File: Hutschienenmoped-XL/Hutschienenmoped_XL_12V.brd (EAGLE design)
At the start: 96.3 x 101.8 mm, 118 parts, among them J1 638207222005, J13 638207222005, J15 638207222008, J2 645004114822, J3 61302211821, J4 61300421121, J6 61302211821, J7 638207222005, J8 638207222007, U1 ESP32-S3-DEVKITC-1-N8R2, U4 TLE9250VSJ

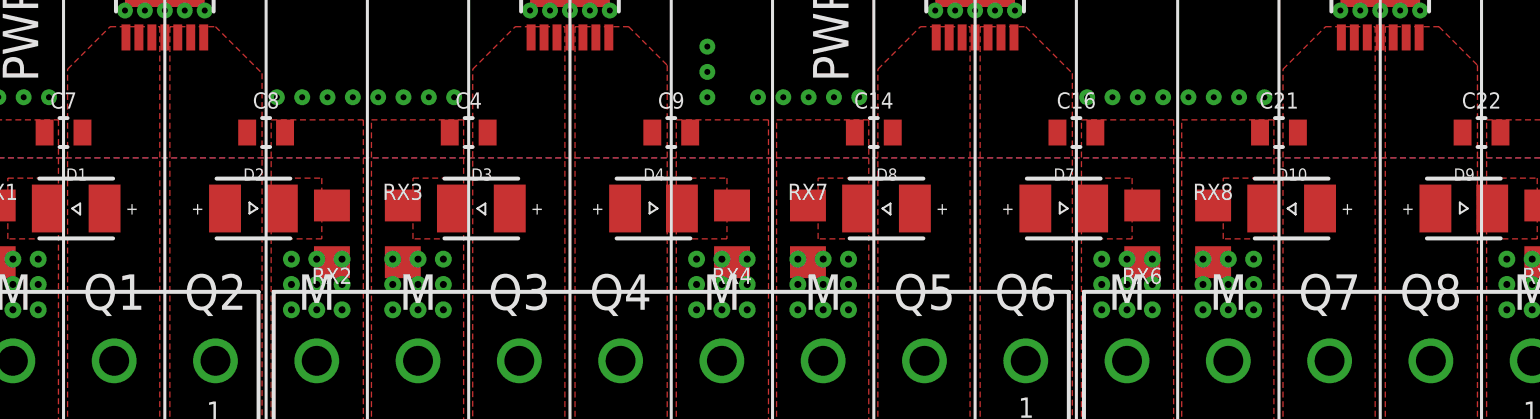
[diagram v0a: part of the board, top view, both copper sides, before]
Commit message: update Libraries.
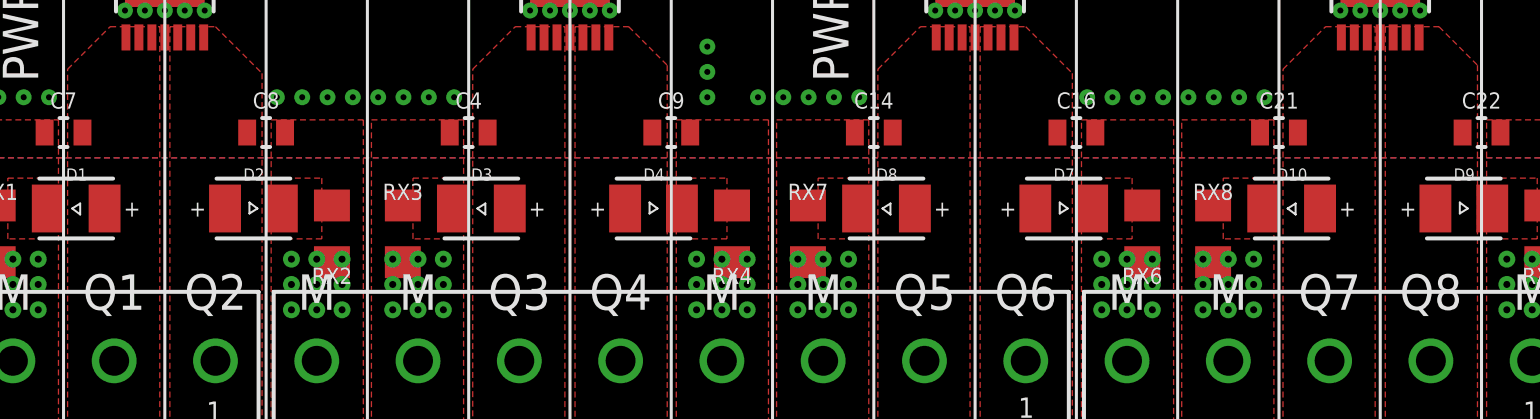
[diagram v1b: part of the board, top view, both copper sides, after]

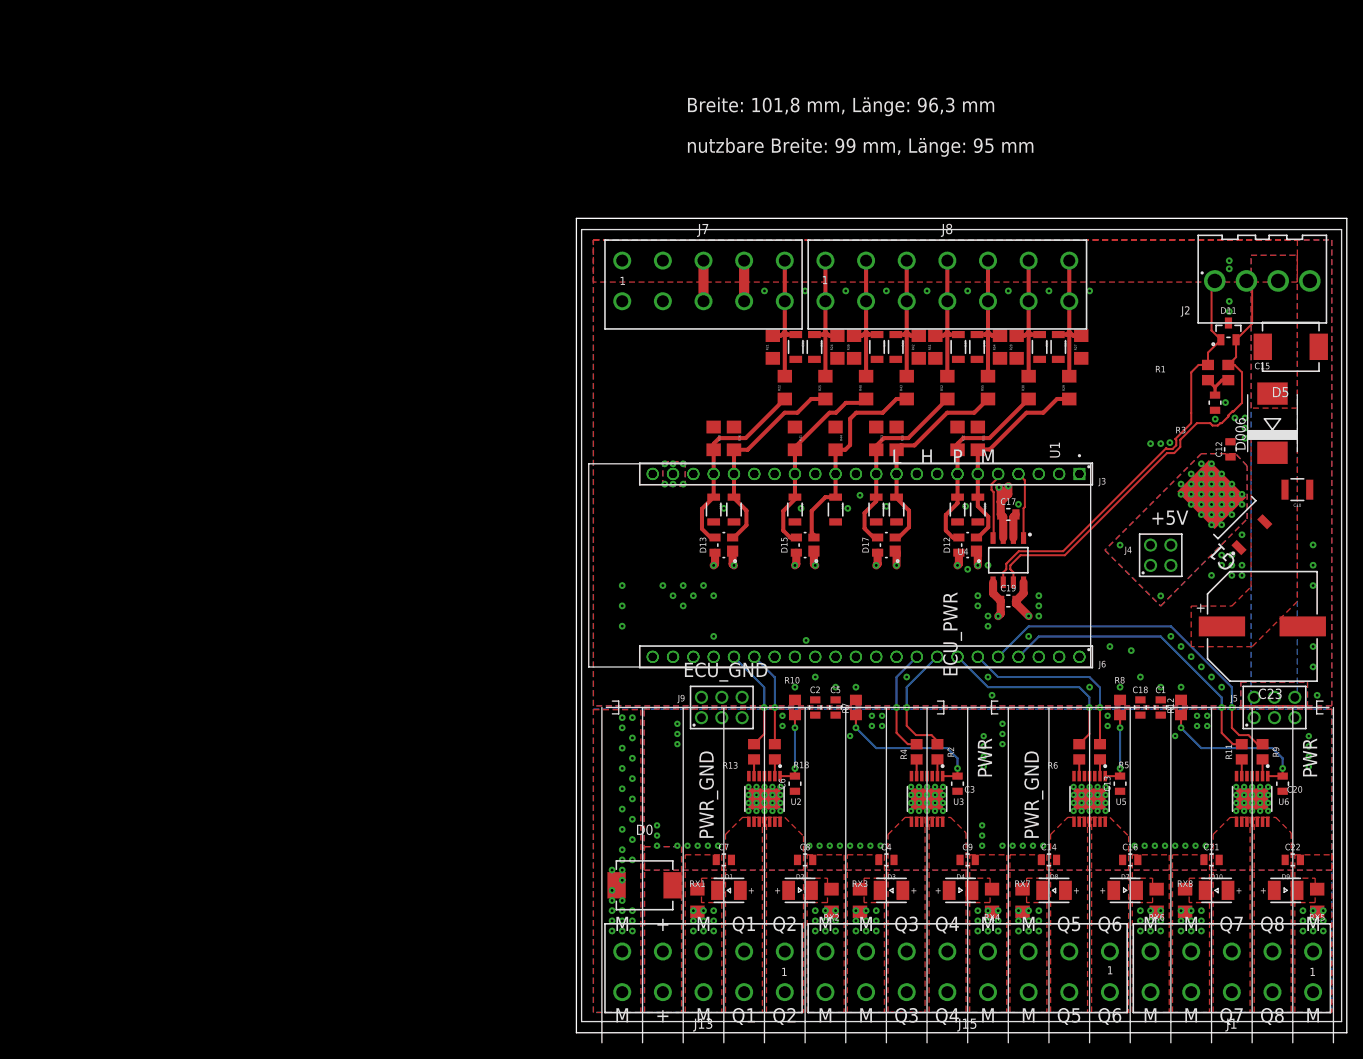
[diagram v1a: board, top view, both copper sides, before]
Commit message: Change grid unit to mm, adjust layer visibility and settings, update Fusion 360 sync status, modify wire connections and text positions.
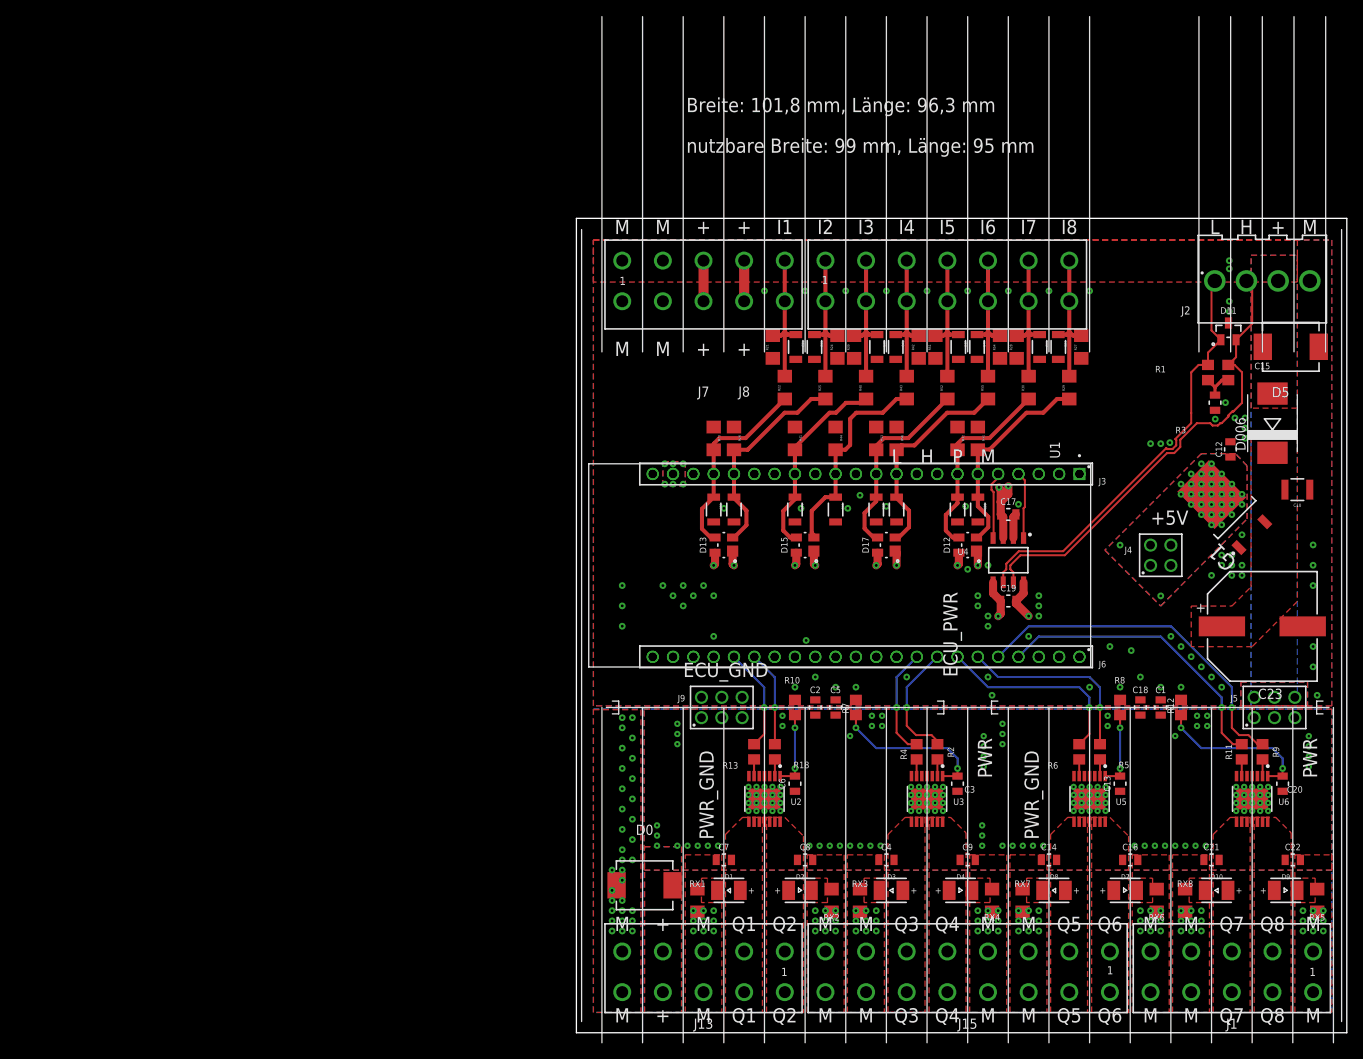
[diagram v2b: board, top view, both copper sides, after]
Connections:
- removed net N$16: J7.2, J7.A2
- removed net N$7: J7.4, J7.A4
- net ECU_GND: now also J7.2, J7.A2
- net ECU_PWR: now also J7.4, J7.A4
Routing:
- net N$7: track 5.08 -> 0.00 mm
- net ECU_PWR: track 5.08 -> 10.2 mm
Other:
- board text added: "I1"
- board text added: "I2"
- board text added: "I3"
- board text added: "I4"
- board text added: "I5"
- board text added: "I6"
- board text added: "I7"
- board text added: "I8"

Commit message: NOT correct !
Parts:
- removed U1: ESP32-S3-DEVKITC-1-N8R2, ESP32-S3-DEVKITC-1-N8R2:XCVR_ESP32-S3-DEVKITC-1-N8R2
- added MP1, MP2, MP3, MP4, MP5, MP6, MP7, MP8: M3 x 2.5mm, Wurth_Assembly_WA-SMSI:WA-SMSI_9774025360
- added R14, R15: 13K, resistor:R1206
- added W1-J1, W2-J1: 61301015721, WE-special:61301015721
- added W1-J2, W2-J2: 61300615721, Wurth_Connectors_WR-PHD:61300615721
- moved D11 1.27 mm to (80.9, 86.4)
- moved D5 1.02 mm to (88.6, 84.7)
- moved R55 0.57 mm to (51.1, 80.1)
- moved C31 0.51 mm to (26.8, 85.2)
- moved R21 0.51 mm to (23.9, 85.2)
- moved R22 0.51 mm to (25.4, 80.1)
- moved R24 0.51 mm to (32.0, 85.2)
- moved R25 0.51 mm to (30.5, 80.1)
- moved R27 0.51 mm to (62.5, 85.2)
- moved R28 0.51 mm to (54.4, 85.2)
- moved R29 0.51 mm to (61.0, 80.1)
- moved R30 0.51 mm to (55.9, 80.1)
- moved R39 0.51 mm to (34.1, 85.2)
- moved R40 0.51 mm to (35.6, 80.1)
- moved R42 0.51 mm to (42.1, 85.2)
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- renumbered J3 to ESP32-J1, J6 to ESP32-J3
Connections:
- removed net IX00: U1.J1_20
- removed net IX06: U1.J1_8
- removed net MB_UART_RTS1: U1.J1_16
- removed net MB_UART_RXD1: U1.J1_12
- removed net MB_UART_RXD2: U1.J1_17
- removed net N$20: J13.5, J13.A5
- removed net QX06: U1.J3_16
- removed net QX07: U1.J3_10
- new net CS0: ESP32-J1.14, W1-J1.6
- new net CS1: ESP32-J1.12, W2-J1.6
- new net INT0: ESP32-J3.16, W1-J2.5
- new net INT1: ESP32-J3.15, W2-J2.5
- new net MISO: ESP32-J1.20, W1-J1.4, W2-J1.4
- new net MOSI: ESP32-J1.17, W1-J1.3, W2-J1.3
- new net RST0: ESP32-J1.9, W1-J2.3
- new net RST1: ESP32-J3.10, W2-J2.3
- new net SCLK: ESP32-J1.16, W1-J1.5, W2-J1.5
- net +3V3: now also ESP32-J1.1, ESP32-J1.2, W1-J1.7, W1-J1.8, W1-J2.1, W2-J1.7, W2-J1.8, W2-J2.1; no longer U1.J1_1, U1.J1_2
- net +5V: now also ESP32-J1.21; no longer U1.J1_21
- net BOOT: now also ESP32-J3.14; no longer U1.J3_14
- net CAN1_RXD: now also ESP32-J1.5; no longer U1.J1_5
- net CAN1_TXD: now also ESP32-J1.4; no longer U1.J1_4
- net CI1: now also ESP32-J1.19; no longer U1.J1_19
- net CI2: now also ESP32-J1.18; no longer U1.J1_18
- net CI3: now also ESP32-J1.15; no longer U1.J1_15
- net CI4: now also ESP32-J1.13; no longer U1.J1_13
- net CI5: now also ESP32-J1.11; no longer U1.J1_11
- net CI6: now also ESP32-J1.10; no longer U1.J1_10
- net CI7: now also ESP32-J1.7; no longer U1.J1_7
- net CI8: now also ESP32-J1.6; no longer U1.J1_6
- net ECU_GND: now also ESP32-J1.22, ESP32-J3.1, ESP32-J3.21, ESP32-J3.22, MP5.1, MP6.1, MP7.1, MP8.1, R14.1, R15.1, W1-J1.1, W1-J1.2, W1-J2.6, W2-J1.1, W2-J1.2, W2-J2.6; no longer U1.J1_22, U1.J3_1, U1.J3_21, U1.J3_22
- net PWR_GND: now also J13.5, J13.A5, MP1.1, MP2.1, MP3.1, MP4.1
- net Q1C: now also ESP32-J3.18; no longer U1.J3_18
- net Q2C: now also ESP32-J3.17, R15.2; no longer U1.J3_17
- net Q3C: now also ESP32-J3.9, R14.2; no longer U1.J3_9
- net Q4C: now also ESP32-J3.8; no longer U1.J3_8
- net Q5C: now also ESP32-J3.7; no longer U1.J3_7
- net Q6C: now also ESP32-J3.6; no longer U1.J3_6
- net Q7C: now also ESP32-J3.4; no longer U1.J3_4
- net Q8C: now also ESP32-J3.5; no longer U1.J3_5
- net RESET: now also ESP32-J1.3; no longer U1.J1_3
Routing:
- net RST0: track 0.00 -> 141.5 mm, vias 0 -> 1
- net CS0: track 0.00 -> 103.1 mm, vias 0 -> 2
- net INT0: track 0.00 -> 103.0 mm
- net SCLK: track 0.00 -> 101.2 mm, vias 0 -> 1
- net MOSI: track 0.00 -> 98.2 mm
- net RST1: track 0.00 -> 95.1 mm, vias 0 -> 1
- net MISO: track 0.00 -> 88.5 mm, vias 0 -> 1
- net INT1: track 0.00 -> 77.0 mm, vias 0 -> 1
- net CS1: track 0.00 -> 68.7 mm, vias 0 -> 2
- net Q3C: track 13.7 -> 15.7 mm, vias 1 -> 0
- net I6: track 17.7 -> 18.6 mm
- net I1: track 17.7 -> 18.6 mm
- net I2: track 17.7 -> 18.5 mm
- net I7: track 17.7 -> 18.5 mm
- net I4: track 17.7 -> 18.5 mm
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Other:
- board size 96.3 x 101.8 mm -> 166.3 x 101.8 mm
- board text added: "ETH 1"
- board text added: "ETH 2"

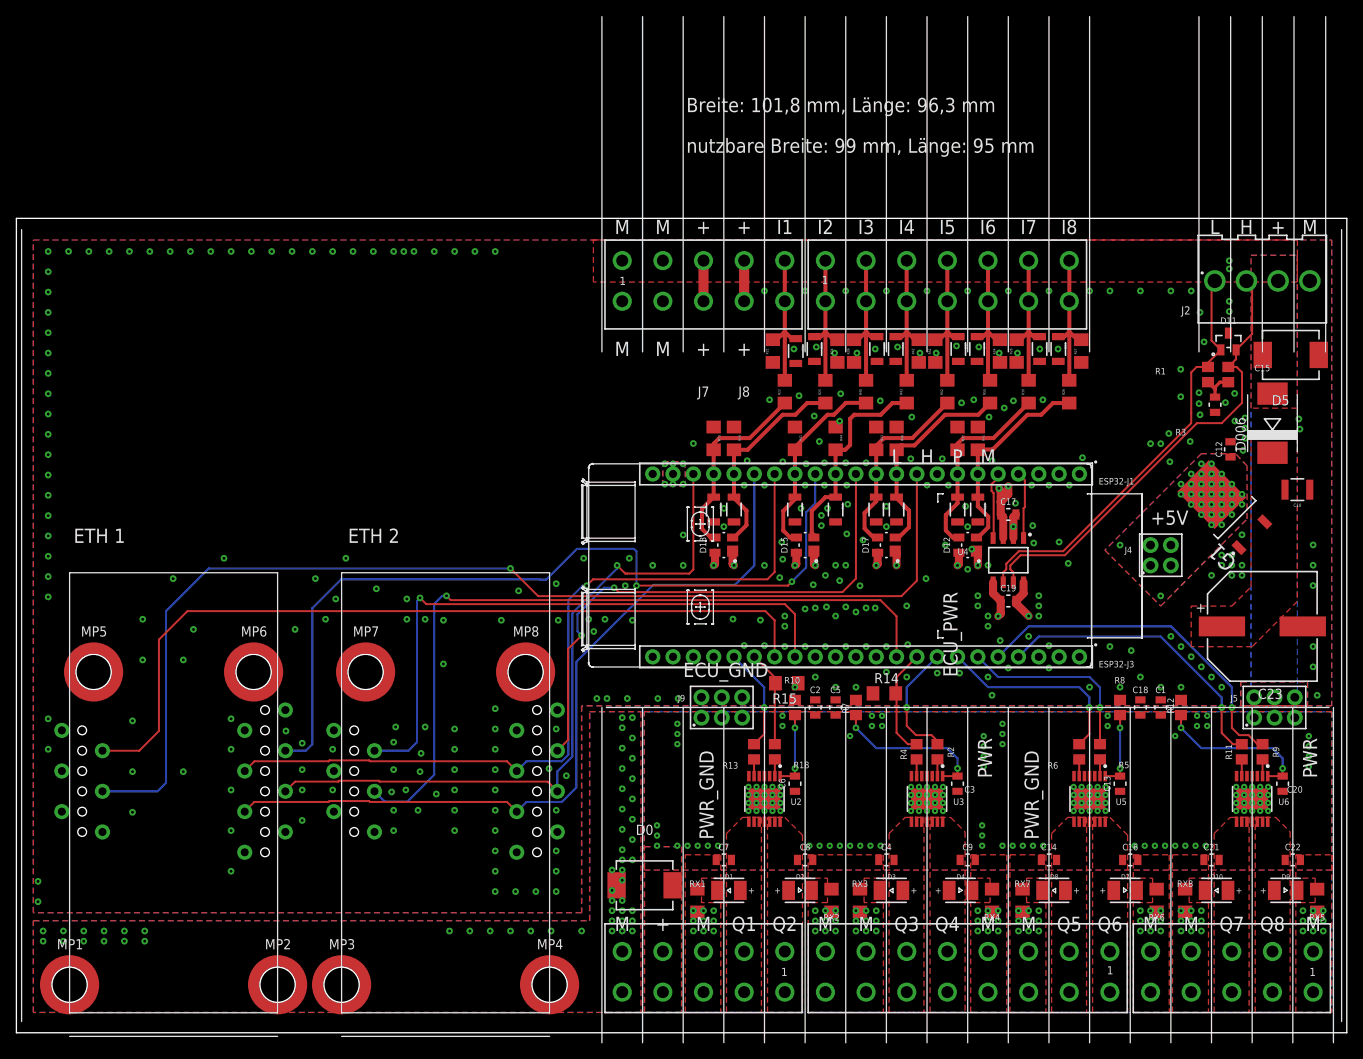
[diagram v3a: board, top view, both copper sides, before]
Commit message: Update grid distance to 70mm, layer visibility adjustments.
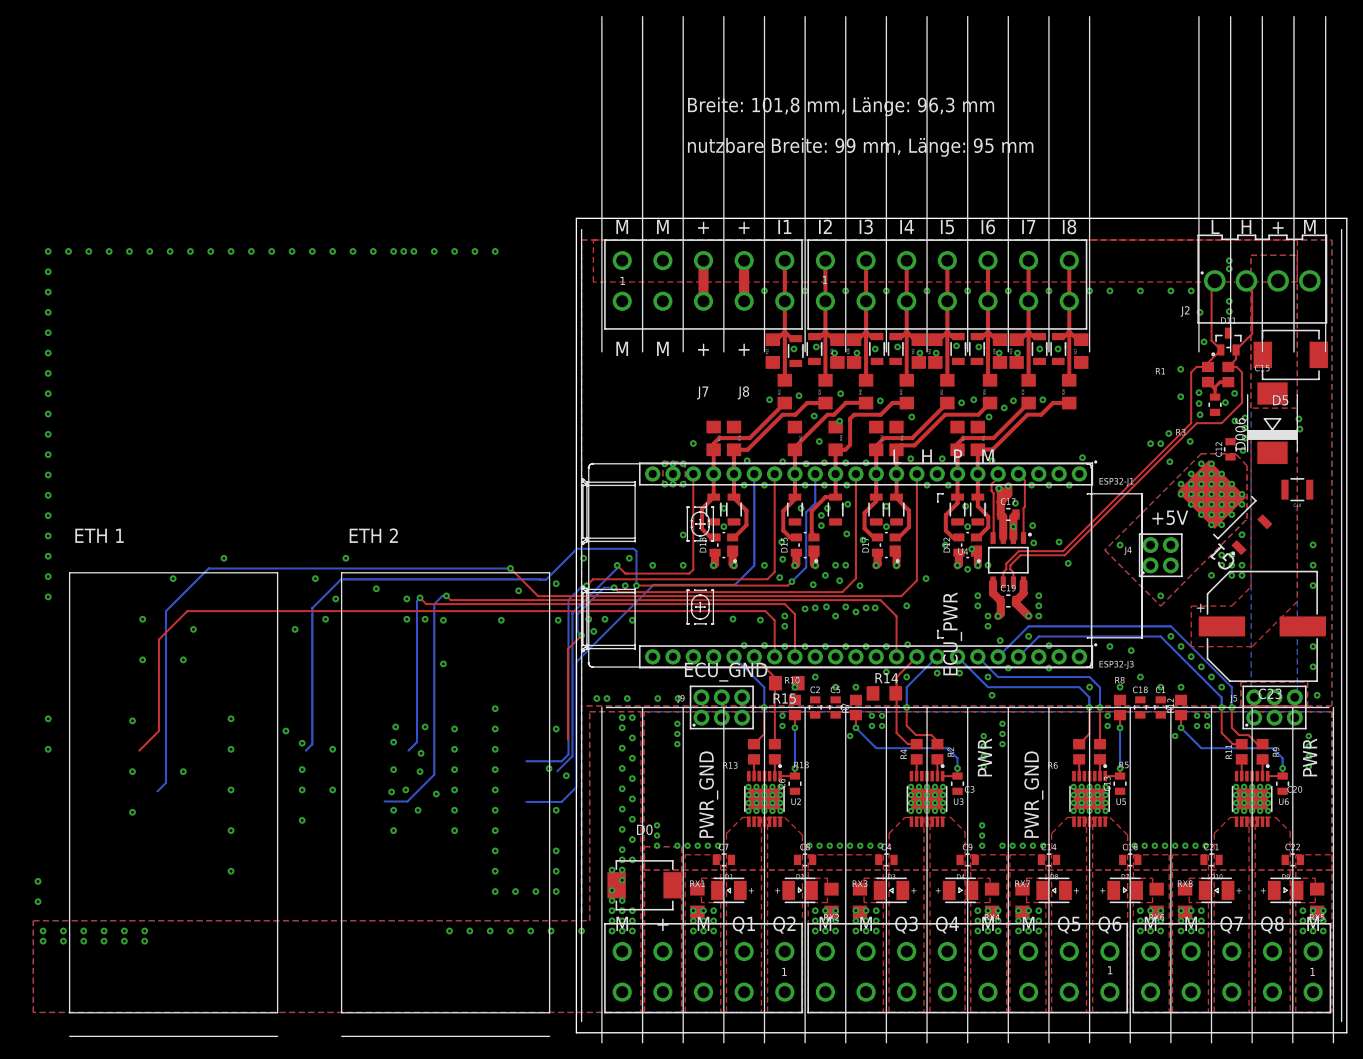
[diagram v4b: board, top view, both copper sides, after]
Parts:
- removed MP1, MP2, MP3, MP4, MP5, MP6, MP7, MP8: M3 x 2.5mm, Wurth_Assembly_WA-SMSI:WA-SMSI_9774025360
- removed W1-J1, W2-J1: 61301015721, WE-special:61301015721
- removed W1-J2, W2-J2: 61300615721, Wurth_Connectors_WR-PHD:61300615721
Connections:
- net +3V3: no longer W1-J1.7, W1-J1.8, W1-J2.1, W2-J1.7, W2-J1.8, W2-J2.1
- net CS0: no longer W1-J1.6
- net CS1: no longer W2-J1.6
- net ECU_GND: no longer MP5.1, MP6.1, MP7.1, MP8.1, W1-J1.1, W1-J1.2, W1-J2.6, W2-J1.1, W2-J1.2, W2-J2.6
- net INT0: no longer W1-J2.5
- net INT1: no longer W2-J2.5
- net MISO: no longer W1-J1.4, W2-J1.4
- net MOSI: no longer W1-J1.3, W2-J1.3
- net PWR_GND: no longer MP1.1, MP2.1, MP3.1, MP4.1
- net RST0: no longer W1-J2.3
- net RST1: no longer W2-J2.3
- net SCLK: no longer W1-J1.5, W2-J1.5
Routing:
- net MISO: track 88.5 -> 50.9 mm
- net SCLK: track 101.2 -> 64.4 mm
- net MOSI: track 98.2 -> 61.3 mm
- net RST0: track 141.5 -> 134.6 mm
- net INT0: track 103.0 -> 98.4 mm
- net INT1: track 77.0 -> 72.7 mm
- net CS0: track 103.1 -> 100.5 mm
- net CS1: track 68.7 -> 66.8 mm
- net RST1: track 95.1 -> 93.3 mm
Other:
- board size 166.3 x 101.8 mm -> 96.3 x 101.8 mm
